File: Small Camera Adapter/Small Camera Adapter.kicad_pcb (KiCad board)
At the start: 2 copper layers, 25 x 25 mm, 10 parts, among them J1 68611514122, J2 10137062-00021LF

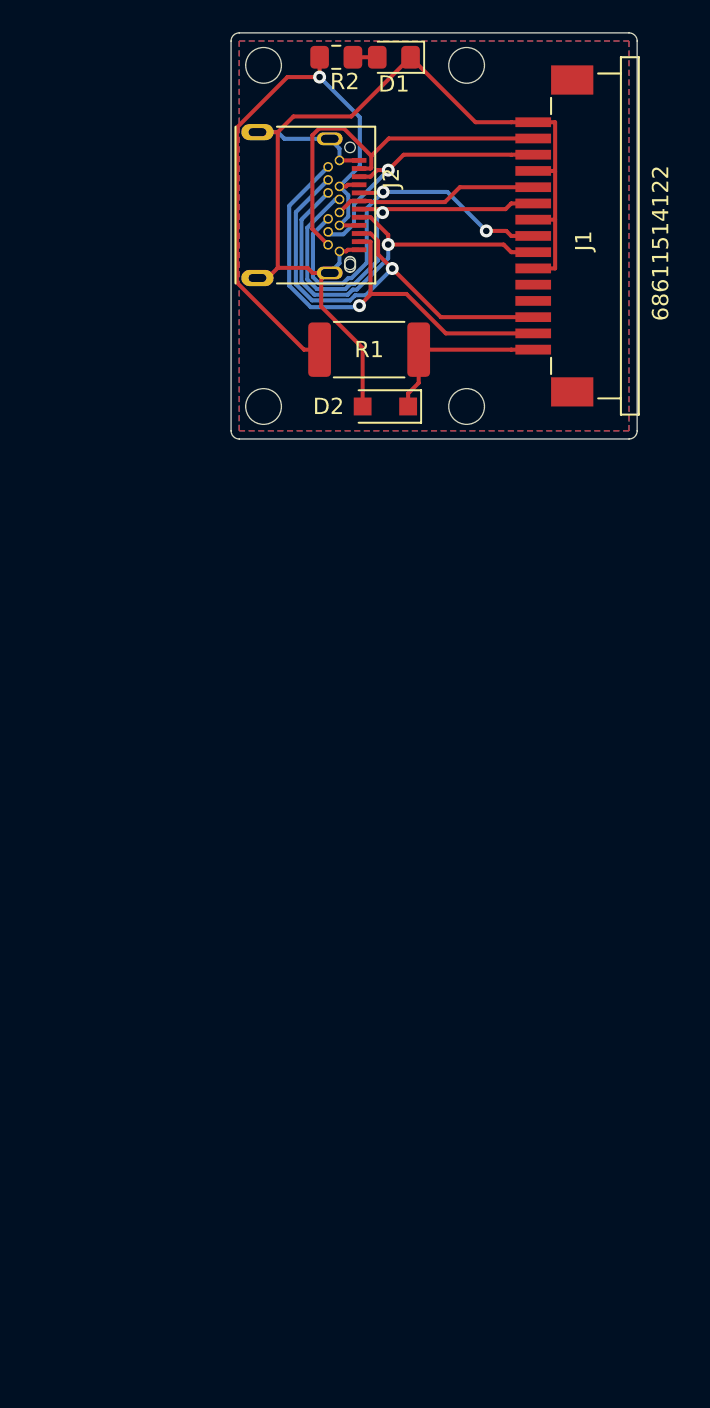
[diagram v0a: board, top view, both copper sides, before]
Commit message: Update to camera adapter
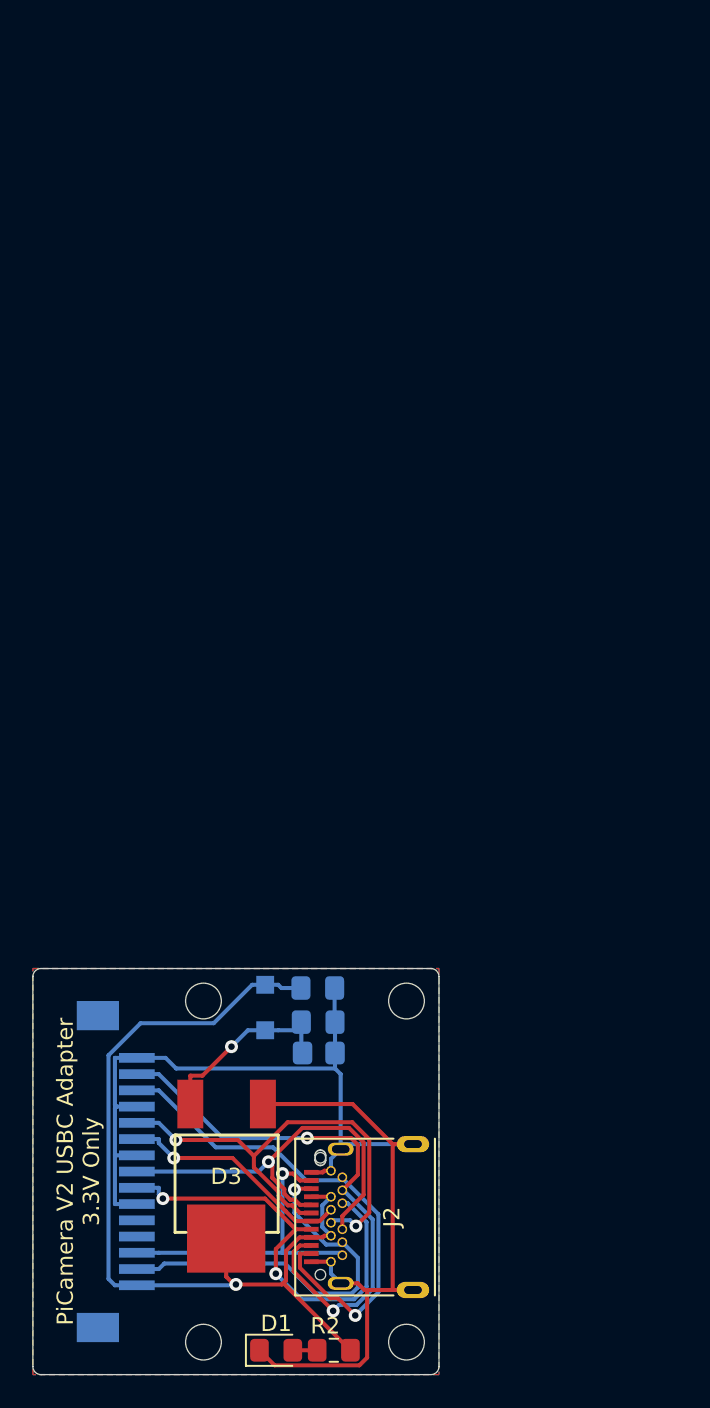
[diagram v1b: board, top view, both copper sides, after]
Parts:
- added C1: 100nF, Capacitor_SMD:C_0805_2012Metric_Pad1.18x1.45mm_HandSolder, B.Cu at (157.8, 109.3)
- added C2: 47nF, Capacitor_SMD:C_0805_2012Metric_Pad1.18x1.45mm_HandSolder, B.Cu at (157.9, 111.4)
- added D3: Q_SCR_KAG, digikey-footprints:DPAK, F.Cu at (152.2, 120.1)
- D2, J1: moved to B.Cu
- R1: value 100R -> 1K; footprint Resistor_SMD:R_2512_6332Metric_Pad1.40x3.35mm_HandSolder -> Resistor_SMD:R_0805_2012Metric_Pad1.20x1.40mm_HandSolder; moved to B.Cu
- moved REF2 80.3 mm to (150.8, 131.1), turned to 180 degrees
- moved D1 79.9 mm to (155.3, 131.6), turned to 0 degrees
- moved R2 79.6 mm to (158.8, 131.6), turned to 180 degrees
- moved REF1 79.1 mm to (163.3, 131.1), turned to 180 degrees
- moved J1 64.6 mm to (144.3, 120.6)
- moved J2 62.3 mm to (158.0, 123.4), turned to 90 degrees
- moved R1 43.4 mm to (157.9, 113.3)
- moved REF3 40.0 mm to (150.8, 110.1), turned to 180 degrees
- moved D2 37.7 mm to (154.6, 110.5), turned to 270 degrees
- moved REF4 37.6 mm to (163.3, 110.1), turned to 180 degrees
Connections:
- D2 pad 2: GND -> Net-(C2-Pad1)
- J2 pad A10: CAMERASCL -> CAMERASDA
- J2 pad A11: CAMERASDA -> CAMERASCL
- J2 pad A2: CAMERADN0 -> CAMERADP0
- J2 pad A3: CAMERADP0 -> CAMERADN0
- J2 pad A4: +3V3 -> 3.3VProtected
- J2 pad A5: CAMERACN -> CAMERACP
- J2 pad A6: CAMERADN1 -> CAMERADP1
- J2 pad A7: CAMERADP1 -> CAMERADN1
- J2 pad A8: CAMERACP -> CAMERACN
- J2 pad A9: +3V3 -> 3.3VProtected
- J2 pad B10: CAMERASCL -> CAMERASDA
- J2 pad B11: CAMERASDA -> CAMERASCL
- J2 pad B2: CAMERADN0 -> CAMERADP0
- J2 pad B3: CAMERADP0 -> CAMERADN0
- J2 pad B4: +3V3 -> 3.3VProtected
- J2 pad B5: CAMERACN -> CAMERACP
- J2 pad B6: CAMERADN1 -> CAMERADP1
- J2 pad B7: CAMERADP1 -> CAMERADN1
- J2 pad B8: CAMERACP -> CAMERACN
- J2 pad B9: +3V3 -> 3.3VProtected
- R1 pad 1: 3.3VProtected -> GND
- R1 pad 2: +3V3 -> Net-(C2-Pad1)
- R2 pad 1: +3V3 -> 3.3VProtected
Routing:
- net 3.3VProtected: track 10.8 -> 56.7 mm, vias 0 -> 1
- net +3V3: track 37.5 -> 0.00 mm, vias 1 -> 0
- net CAMERADN1: track 12.6 -> 29.4 mm, vias 0 -> 2
- net GND: track 67.7 -> 82.2 mm
- net CAMERADP0: track 17.4 -> 31.2 mm
- net Net-(C2-Pad1): track 0.00 -> 11.7 mm, vias 0 -> 1
- net CAMERADP1: track 25.4 -> 14.5 mm
- net CAMERADN0: track 23.6 -> 34.4 mm, vias 0 -> 2
- net CAMERASCL: track 27.7 -> 19.5 mm
- net CAMERASDA: track 29.2 -> 24.2 mm
- net CAMERACP: track 25.5 -> 27.8 mm, vias 1 -> 2
- net CAMERACN: track 24.6 -> 25.7 mm, vias 2 -> 1
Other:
- board text added: "PiCamera V2 USBC Adapter 3.3V Only"
